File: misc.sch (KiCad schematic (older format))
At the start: 13 parts, among them J12 Conn_02x03_Odd_Even, U18 AZ1117-5.0, U19 RP117, U20 MIC5317, U21 L78L33_SO8

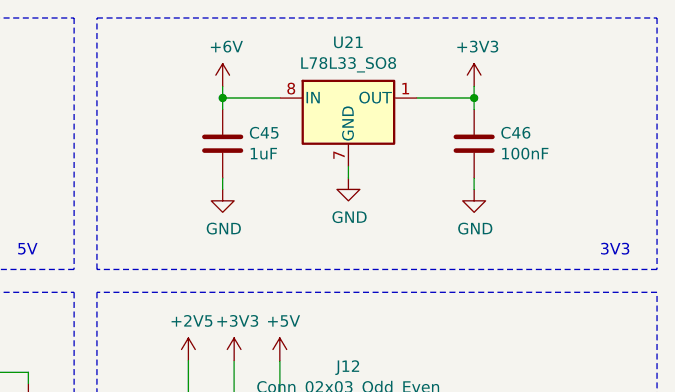
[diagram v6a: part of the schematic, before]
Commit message: replaced 78xx series 3V3 regulator  for 1117 series
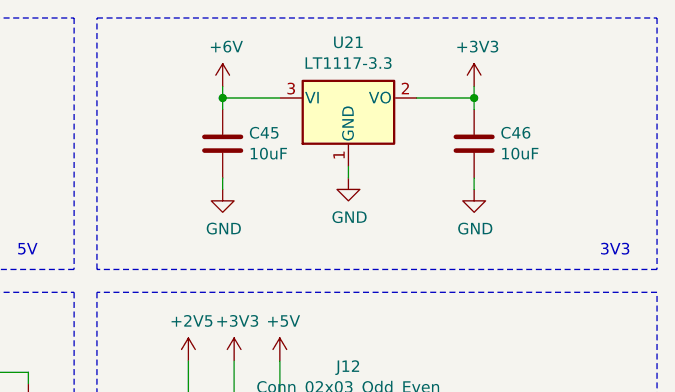
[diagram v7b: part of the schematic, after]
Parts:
- removed U21: L78L33_SO8, Package_SO:SOIC-8_3.9x4.9mm_P1.27mm, symbol Regulator_Linear:L78L33_SO8
- added U21: LT1117-3.3, Package_TO_SOT_SMD:SOT-223-3_TabPin2, symbol Regulator_Linear:LT1117-3.3
- C45: value 1uF -> 10uF
- C46: value 100nF -> 10uF
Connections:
- net +3V3: now also U21.2 (VO)
- net +6V: now also U21.3 (VI)
- net GND: now also U21.1 (GND)
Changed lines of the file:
@@
 P 8850 2550
 F 0 "C46" H 8965 2596 50  0000 L CNN
-F 1 "100nF" H 8965 2505 50  0000 L CNN
+F 1 "10uF" H 8965 2505 50  0000 L CNN
 F 2 "Capacitor_SMD:C_0603_1608Metric_Pad1.08x0.95mm_HandSolder" H 8888 2400 50  0001 C CNN
 F 3 "~" H 8850 2550 50  0001 C CNN
@@
 P 7750 2550
 F 0 "C45" H 7865 2596 50  0000 L CNN
-F 1 "1uF" H 7865 2505 50  0000 L CNN
+F 1 "10uF" H 7865 2505 50  0000 L CNN
 F 2 "Capacitor_SMD:C_0603_1608Metric_Pad1.08x0.95mm_HandSolder" H 7788 2400 50  0001 C CNN
 F 3 "~" H 7750 2550 50  0001 C CNN
@@
 Text Notes 9400 3050 0    50   ~ 0
 3V3\n
-$Comp
-L Regulator_Linear:L78L33_SO8 U21
-U 1 1 60631119
-P 8300 2350
-F 0 "U21" H 8300 2592 50  0000 C CNN
-F 1 "L78L33_SO8" H 8300 2501 50  0000 C CNN
-F 2 "Package_SO:SOIC-8_3.9x4.9mm_P1.27mm" H 8400 2550 50  0001 C CIN
-F 3 "http://www.st.com/content/ccc/resource/technical/document/datasheet/15/55/e5/aa/23/5b/43/fd/CD00000446.pdf/files/CD00000446.pdf/jcr:content/translations/en.CD00000446.pdf" H 8500 2350 50  0001 C CNN
-	1    8300 2350
-	1    0    0    -1
-$EndComp
 $Comp
 L power:+3V3 #PWR071
@@
 Wire Wire Line
 	8850 3850 8850 3950
+$Comp
+L Regulator_Linear:LT1117-3.3 U21
+U 1 1 606CDFC4
+P 8300 2350
+F 0 "U21" H 8300 2592 50  0000 C CNN
+F 1 "LT1117-3.3" H 8300 2501 50  0000 C CNN
+F 2 "Package_TO_SOT_SMD:SOT-223-3_TabPin2" H 8300 2350 50  0001 C CNN
+F 3 "https://www.analog.com/media/en/technical-documentation/data-sheets/1117fd.pdf" H 8300 2350 50  0001 C CNN
+	1    8300 2350
+	1    0    0    -1
+$EndComp
 $EndSCHEMATC
